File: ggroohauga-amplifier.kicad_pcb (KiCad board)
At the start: 2 copper layers, 85.3 x 31 mm, 4 parts

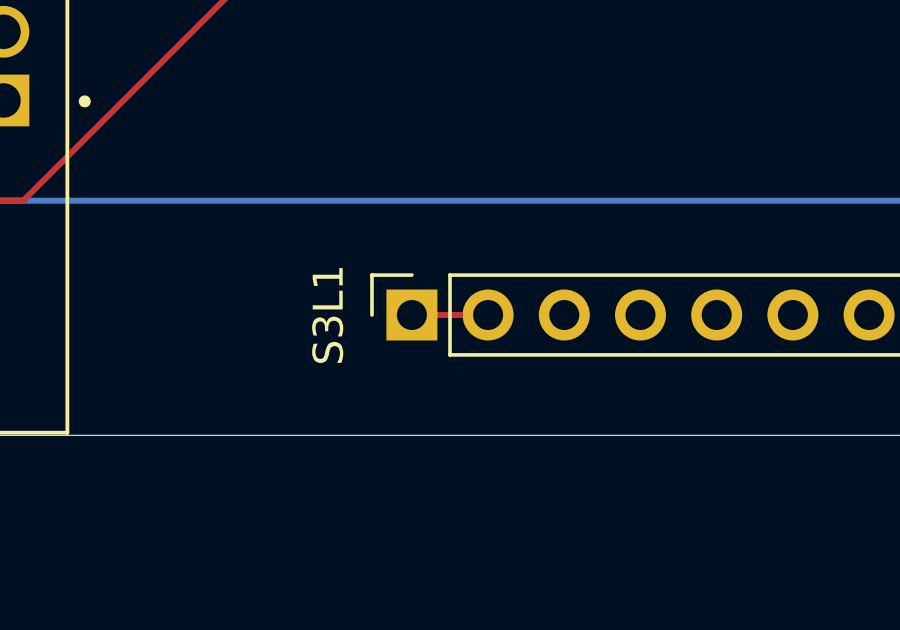
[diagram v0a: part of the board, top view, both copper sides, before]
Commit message: Fix compatibility with ESP32-S3-DevKitM-1
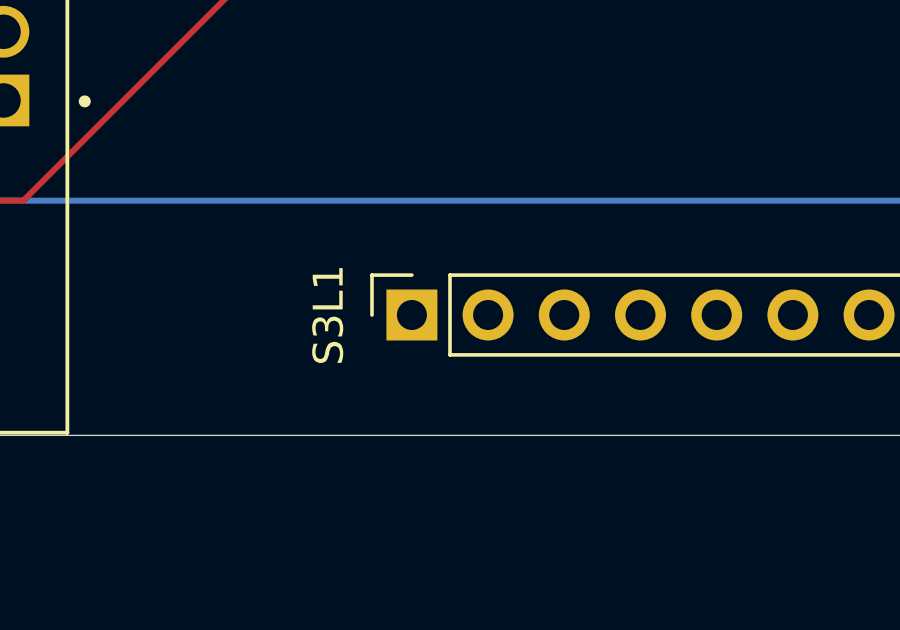
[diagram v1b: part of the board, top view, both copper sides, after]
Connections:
- S3L1 pad 2: +3.3V -> unconnected-(S3L1-Pin_2-Pad2)
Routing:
- net +3.3V: track 2.54 -> 0.00 mm
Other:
- board text added: "urn:oid:1.3.6.1.4.1.39777.1.3.1.1.1 https://github.com/nomis/ggroohauga-pcb (amplifier)"
- board text removed: "urn:oid:1.3.6.1.4.1.39777.1.3.1.1.0 https://github.com/nomis/ggroohauga-pcb (amplifier)"
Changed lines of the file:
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@@
 	(net 48 "unconnected-(S3R1-Pin_15-Pad15)")
 	(net 49 "unconnected-(S3R1-Pin_19-Pad19)")
+	(net 50 "unconnected-(S3L1-Pin_2-Pad2)")
 	(footprint "Connector_PinSocket_2.54mm:PinSocket_1x20_P2.54mm_Vertical"
 		(layer "F.Cu")
@@
 			)
 			(remove_unused_layers no)
-			(net 21 "+3.3V")
+			(net 50 "unconnected-(S3L1-Pin_2-Pad2)")
 			(pinfunction "Pin_2")
-			(pintype "passive")
+			(pintype "passive+no_connect")
 		)
 		(pad "3" thru_hole oval
@@
 		)
 	)
-	(gr_text "urn:oid:1.3.6.1.4.1.39777.1.3.1.1.0\nhttps://github.com/nomis/ggroohauga-pcb\n(amplifier)\n"
+	(gr_text "urn:oid:1.3.6.1.4.1.39777.1.3.1.1.1\nhttps://github.com/nomis/ggroohauga-pcb\n(amplifier)\n"
 		(at 131.064 66.04 0)
 		(layer "B.SilkS")
@@
 		(net 16)
 	)
-	(segment
-		(start 81.534 77.47)
-		(end 84.074 77.47)
-		(width 0.2)
-		(layer "F.Cu")
-		(net 21)
-	)
 	(zone

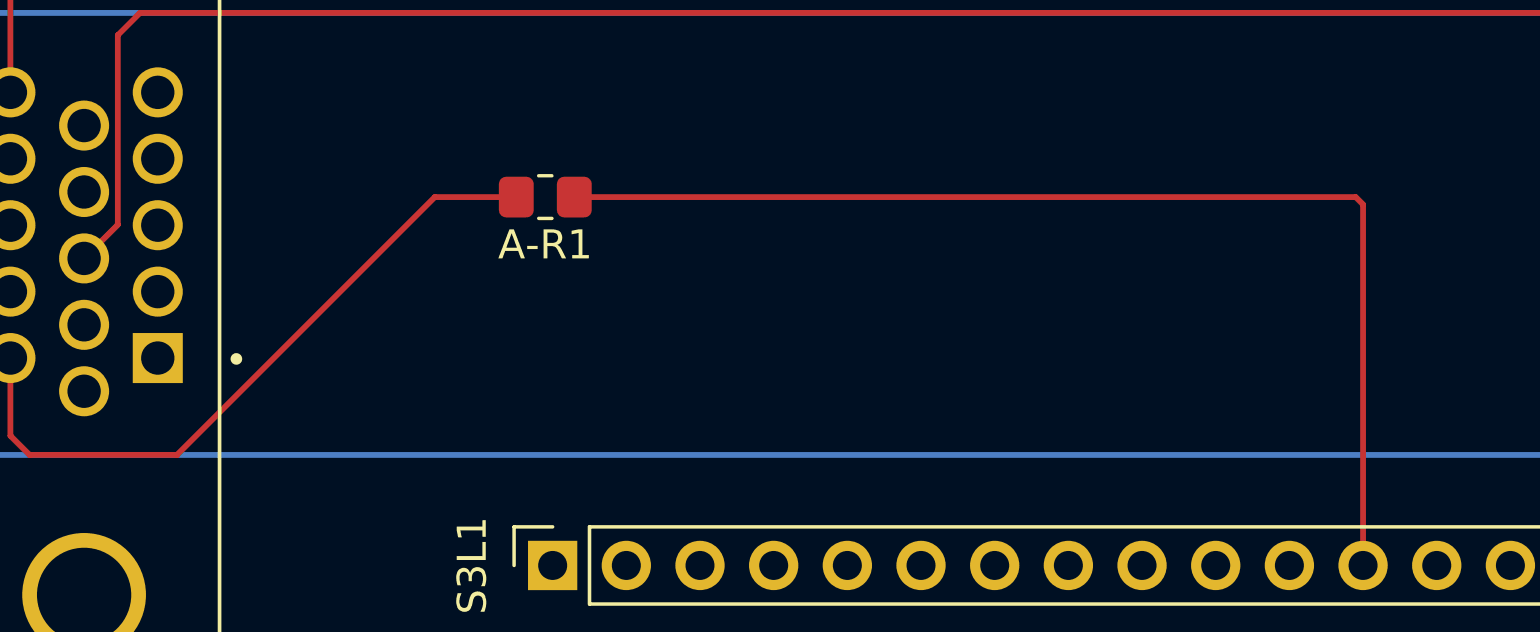
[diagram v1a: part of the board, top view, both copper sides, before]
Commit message: Move resistor on the amplifier too
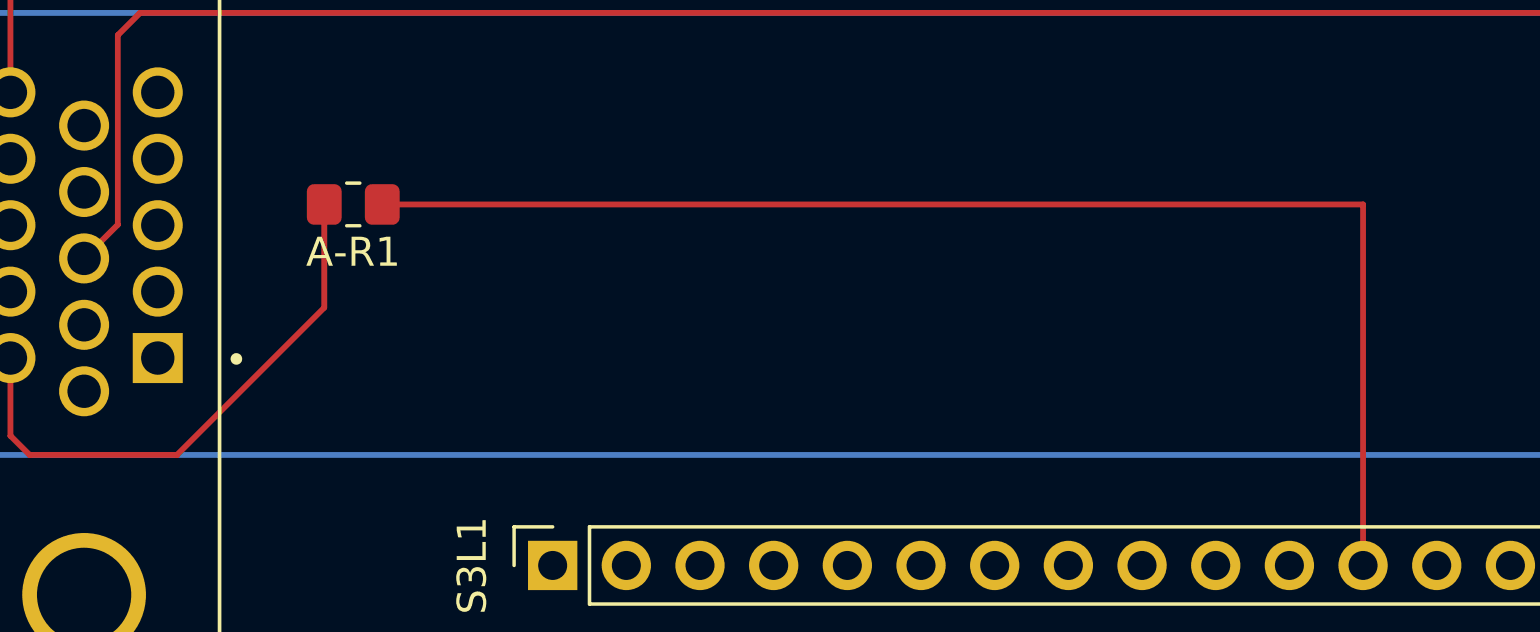
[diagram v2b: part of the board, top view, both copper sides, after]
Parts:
- moved A-R1 6.62 mm to (74.7, 65.0)
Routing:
- net /GPIO_L8_C8_M10/AMP_POWER_IN: track 39.7 -> 46.3 mm
- net /AMP_POWER_IN: track 24.1 -> 19.4 mm
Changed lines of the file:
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@@
 	(footprint "Resistor_SMD:R_0805_2012Metric_Pad1.20x1.40mm_HandSolder"
 		(layer "F.Cu")
-		(at 81.28 64.77 180)
+		(at 74.66 65.024 180)
 		(descr "Resistor SMD 0805 (2012 Metric), square (rectangular) end terminal, IPC_7351 nominal with elongated pad for handsoldering. (Body size source: IPC-SM-782 page 72, https://www.pcb-3d.com/wordpress/wp-content/uploads/ipc-sm-782a_amendment_1_and_2.pdf), generated with kicad-footprint-generator")
 		(tags "resistor handsolder")
@@
 	)
 	(segment
+		(start 73.66 65.024)
+		(end 73.66 68.58)
+		(width 0.2)
+		(layer "F.Cu")
+		(net 5)
+	)
+	(segment
 		(start 68.58 73.66)
 		(end 63.5 73.66)
@@
 	)
 	(segment
-		(start 77.47 64.77)
-		(end 68.58 73.66)
-		(width 0.2)
-		(layer "F.Cu")
-		(net 5)
-	)
-	(segment
-		(start 80.28 64.77)
-		(end 77.47 64.77)
-		(width 0.2)
-		(layer "F.Cu")
-		(net 5)
-	)
-	(segment
 		(start 63.5 73.66)
 		(end 62.8396 72.9996)
@@
 	)
 	(segment
+		(start 73.66 68.58)
+		(end 68.58 73.66)
+		(width 0.2)
+		(layer "F.Cu")
+		(net 5)
+	)
+	(segment
 		(start 59.69 58.42)
 		(end 59.69 64.77)
@@
 	)
 	(segment
-		(start 109.22 64.77)
-		(end 82.28 64.77)
+		(start 75.66 65.024)
+		(end 109.474 65.024)
 		(width 0.2)
 		(layer "F.Cu")
@@
 		(width 0.2)
 		(layer "F.Cu")
-		(net 16)
-	)
-	(segment
-		(start 109.474 65.024)
-		(end 109.22 64.77)
-		(width 0.2)
-		(layer "F.Cu")

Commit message: Fix DE-15 connector footprint so that the shield is automatically GND
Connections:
- A-J1 pad 1: unconnected-(A-J1-Pad1) -> AUDIO_HEADPHONES_R
- A-J1 pad 2: unconnected-(A-J1-Pad2) -> AUDIO_HEADPHONES_L
- A-J1 pad 3: unconnected-(A-J1-Pad3) -> AUDIO_GROUND
- A-J1 pad 4: unconnected-(A-J1-Pad4) -> AUDIO_AUX_R
- A-J1 pad 5: unconnected-(A-J1-Pad5) -> AUDIO_AUX_L

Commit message: Cleanup tracks
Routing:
- net GND: track 0.76 -> 0.00 mm
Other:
- board text added: "urn:oid:1.3.6.1.4.1.39777.1.3.1.1.2 https://github.com/nomis/ggroohauga-pcb (amplifier)"
- board text removed: "urn:oid:1.3.6.1.4.1.39777.1.3.1.1.1 https://github.com/nomis/ggroohauga-pcb (amplifier)"
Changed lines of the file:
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@@
 		)
 	)
-	(gr_text "urn:oid:1.3.6.1.4.1.39777.1.3.1.1.1\nhttps://github.com/nomis/ggroohauga-pcb\n(amplifier)\n"
+	(gr_text "urn:oid:1.3.6.1.4.1.39777.1.3.1.1.2\nhttps://github.com/nomis/ggroohauga-pcb\n(amplifier)\n"
 		(at 131.064 66.04 0)
 		(layer "B.SilkS")
@@
 	)
 	(segment
-		(start 112.014 54.61)
-		(end 111.76 54.61)
-		(width 0.2)
-		(layer "F.Cu")
-		(net 4)
-	)
-	(segment
 		(start 111.76 57.15)
 		(end 63.5 57.15)
@@
 	)
 	(segment
-		(start 62.84825 68.035)
-		(end 62.84825 67.96175)
-		(width 0.2)
-		(layer "F.Cu")
-		(net 7)
-	)
-	(segment
 		(start 60.2408 68.0292)
 		(end 59.69 68.58)
@@
 	)
 	(segment
-		(start 116.84 77.47)
-		(end 117.094 77.47)
-		(width 0.2)
-		(layer "B.Cu")
-		(net 7)
-	)
-	(segment
 		(start 116.84 73.66)
 		(end 116.84 77.47)
@@
 	)
 	(segment
-		(start 65.38825 71.47)
-		(end 65.12 71.47)
-		(width 0.2)
-		(layer "F.Cu")
-		(net 10)
-	)
-	(segment
-		(start 65.12 71.47)
-		(end 64.77 71.12)
-		(width 0.2)
-		(layer "F.Cu")
-		(net 10)
-	)
-	(segment

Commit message: Convert to KiCad 9.0 format
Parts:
- A-J1: value DE15_Receptacle_HighDensity_MountingHoles -> DE15_Socket_HighDensity_MountingHoles

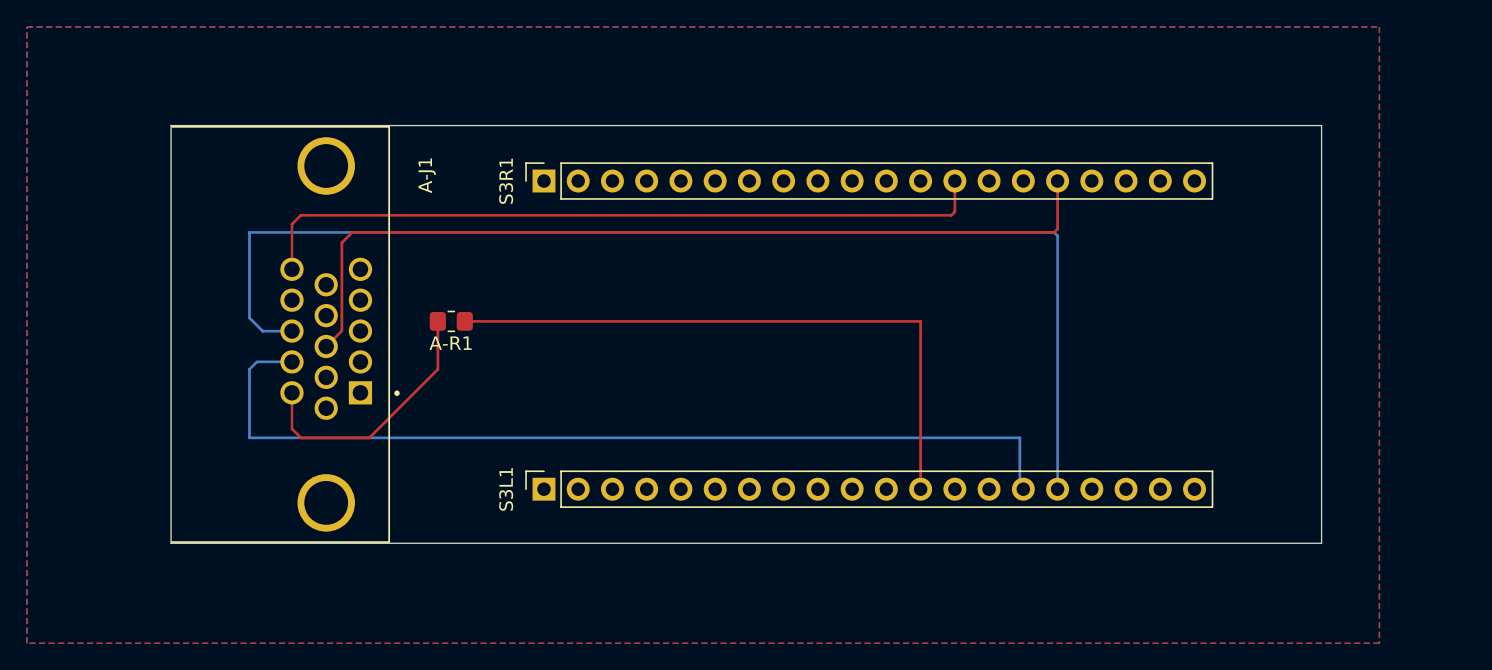
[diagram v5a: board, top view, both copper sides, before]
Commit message: Add 4ch digital isolator and 2 TRS jacks to the amplifier PCB
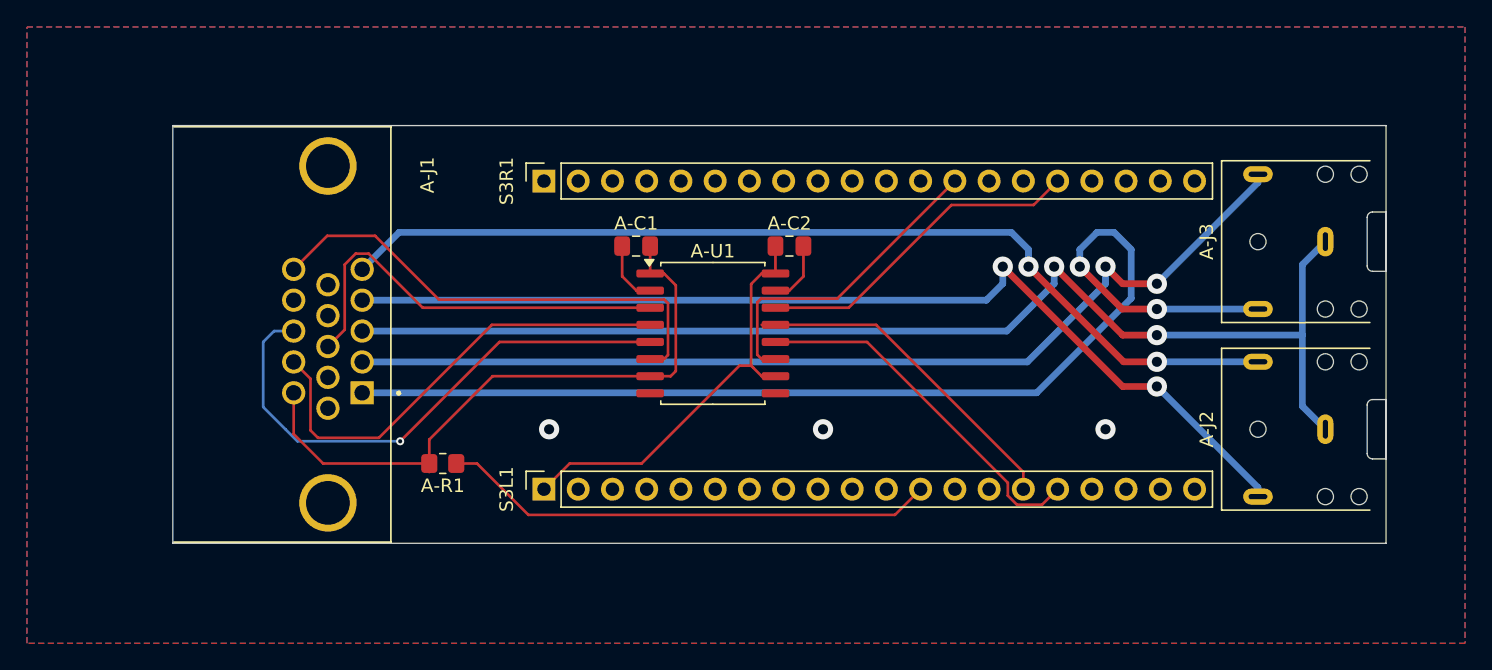
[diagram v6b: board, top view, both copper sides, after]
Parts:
- added A-C1: 0.1µF, Capacitor_SMD:C_0805_2012Metric_Pad1.18x1.45mm_HandSolder, F.Cu at (88.4, 59.4)
- added A-C2: 0.1µF, Capacitor_SMD:C_0805_2012Metric_Pad1.18x1.45mm_HandSolder, F.Cu at (99.7, 59.4)
- added A-J2: Aux In, ggroohauga:Jack_3.5mm_CUI_SJ1-3523N_Horizontal, F.Cu at (139.5, 73.0)
- added A-J3: Headphones, ggroohauga:Jack_3.5mm_CUI_SJ1-3523N_Horizontal, F.Cu at (139.5, 59.1)
- added A-U1: ISO6742, Package_SO:SOIC-16W_7.5x10.3mm_P1.27mm, F.Cu at (94.1, 65.9)
- moved A-R1 10.6 mm to (74.0, 75.6)
- moved A-J1 0.13 mm to (65.5, 66.0)
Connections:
- A-J1 pad 12: /GPIO_L9_C9_M13/AMP_TX -> /AMP_TX
- A-J1 pad 13: /GPIO_L10_C10_M14/AMP_RX -> /AMP_RX
- A-J1 pad 15: /GPIO_L48_C35_M36/CON_ANNOUNCE -> /CON_ANNOUNCE
- A-J1 pad 8: /GPIO_L14_C48_M33/AMP_DETECT -> /AMP_DETECT
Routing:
- net AUDIO_GROUND: track 0.00 -> 89.9 mm, vias 0 -> 2
- net AUDIO_HEADPHONES_R: track 0.00 -> 84.2 mm, vias 0 -> 2
- net AUDIO_AUX_R: track 0.00 -> 75.7 mm, vias 0 -> 2
- net AUDIO_HEADPHONES_L: track 0.00 -> 74.4 mm, vias 0 -> 2
- net AUDIO_AUX_L: track 0.00 -> 72.3 mm, vias 0 -> 2
- net /GPIO_L10_C10_M14/AMP_RX: track 88.8 -> 27.0 mm
- net /GPIO_L9_C9_M13/AMP_TX: track 69.4 -> 25.2 mm
- net /GPIO_L14_C48_M33/AMP_DETECT: track 65.2 -> 24.8 mm
- net /AMP_RX: track 0.00 -> 40.2 mm, vias 0 -> 1
- net /CON_ANNOUNCE: track 0.00 -> 36.2 mm
- net /AMP_TX: track 0.00 -> 34.5 mm
- net +3.3V: track 0.00 -> 31.5 mm
- net /GPIO_L48_C35_M36/CON_ANNOUNCE: track 55.2 -> 23.7 mm
- net /AMP_DETECT: track 0.00 -> 31.2 mm
- net /AMP_POWER_IN: track 19.4 -> 47.5 mm
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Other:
- board size 85.3 x 31 mm -> 90 x 31 mm
- board text added: "urn:oid:1.3.6.1.4.1.39777.1.3.1.1.3 https://github.com/nomis/ggroohauga-pcb (amplifier)"
- board text removed: "urn:oid:1.3.6.1.4.1.39777.1.3.1.1.2 https://github.com/nomis/ggroohauga-pcb (amplifier)"

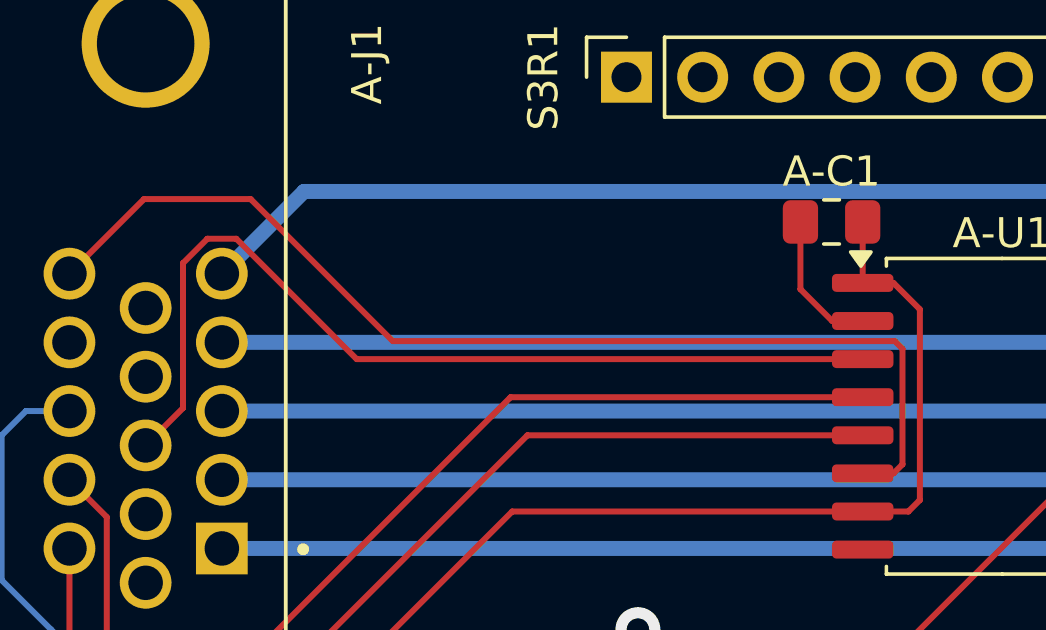
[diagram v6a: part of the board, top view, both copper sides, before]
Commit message: Reorganise schematic into multiple sheets and add 3 board identifier GPIOs
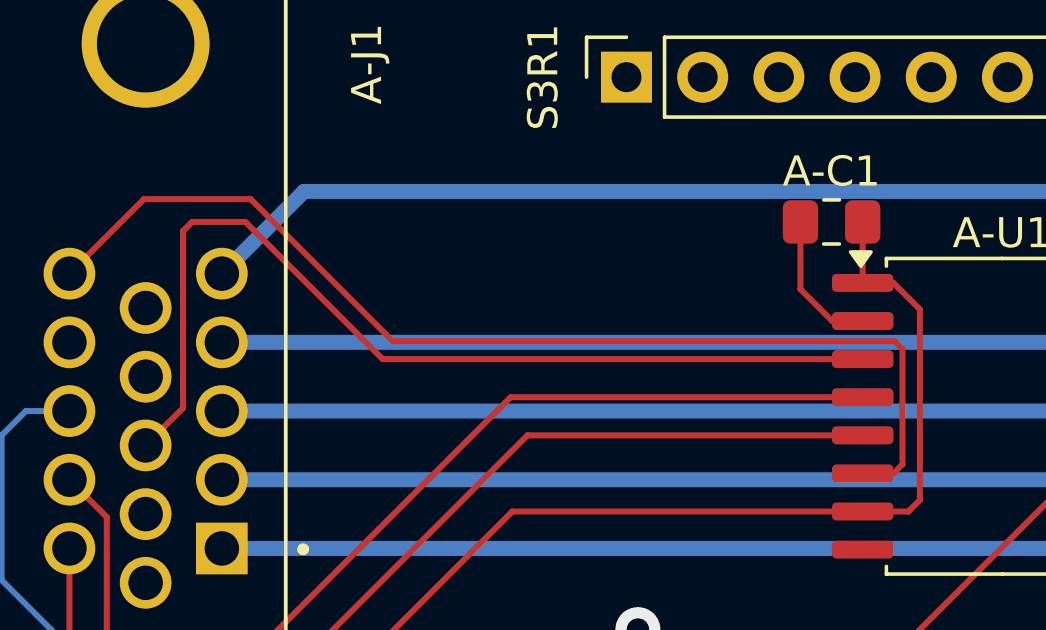
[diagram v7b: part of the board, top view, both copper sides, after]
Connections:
- net /AMP_DETECT renamed /Common/AMP_DETECT
- net /AMP_POWER_IN renamed /Common/AMP_POWER_IN
- net /AMP_RX renamed /Common/AMP_RX
- net /AMP_TX renamed /Common/AMP_TX
- net /CON_ANNOUNCE renamed /Common/CON_ANNOUNCE
- net /GPIO_L10_C10_M14/AMP_RX renamed /Common/GPIO_L10_C10_M14/AMP_RX
- net /GPIO_L13_C47_M26/AMP_ANNOUNCE renamed /Common/GPIO_L13_C47_M26/AMP_ANNOUNCE
- net /GPIO_L14_C48_M33/AMP_DETECT renamed /Common/GPIO_L14_C48_M33/AMP_DETECT
- net /GPIO_L17_C17_M8/CON_DETECT renamed /Common/GPIO_L17_C17_M8/CON_DETECT
- net /GPIO_L40_C40_M41/CON_POWER_OUT renamed /Common/GPIO_L40_C40_M41/CON_POWER_OUT
- net /GPIO_L48_C35_M36/CON_ANNOUNCE renamed /Common/GPIO_L48_C35_M36/CON_ANNOUNCE
- net /GPIO_L4_C4_M2/CON_RX renamed /Common/GPIO_L4_C4_M2/CON_RX
- net /GPIO_L6_C6_M4/CON_TX renamed /Common/GPIO_L6_C6_M4/CON_TX
- net /GPIO_L8_C8_M10/AMP_POWER_IN renamed /Common/GPIO_L8_C8_M10/AMP_POWER_IN
- net /GPIO_L9_C9_M13/AMP_TX renamed /Common/GPIO_L9_C9_M13/AMP_TX
- S3L1 pad 11: unconnected-(S3L1-Pin_11-Pad11) -> GPIO_L18_C18_M9
- S3L1 pad 17: unconnected-(S3L1-Pin_17-Pad17) -> GPIO_L11_C11_M15
- S3L1 pad 18: unconnected-(S3L1-Pin_18-Pad18) -> GPIO_L12_C12_M16
- S3L1 pad 7: unconnected-(S3L1-Pin_7-Pad7) -> GND
- S3L1 pad 8: unconnected-(S3L1-Pin_8-Pad8) -> GND
- S3L1 pad 9: unconnected-(S3L1-Pin_9-Pad9) -> GND
- S3R1 pad 14: unconnected-(S3R1-Pin_14-Pad14) -> GPIO_L47_C47_M35
- S3R1 pad 15: unconnected-(S3R1-Pin_15-Pad15) -> GPIO_L21_C21_M21
- S3R1 pad 7: unconnected-(S3R1-Pin_7-Pad7) -> GPIO_L41_C41_M42
- S3R1 pad 9: unconnected-(S3R1-Pin_9-Pad9) -> GPIO_L39_C39_M40
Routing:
- net /Common/AMP_DETECT: track 31.2 -> 32.3 mm
